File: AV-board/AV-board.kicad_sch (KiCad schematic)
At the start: 25 parts, among them J1 Mini-DIN-8, Q1 BC547, Q2 BC547, Q3 BC547, Q4 BC547, U2 74LS241

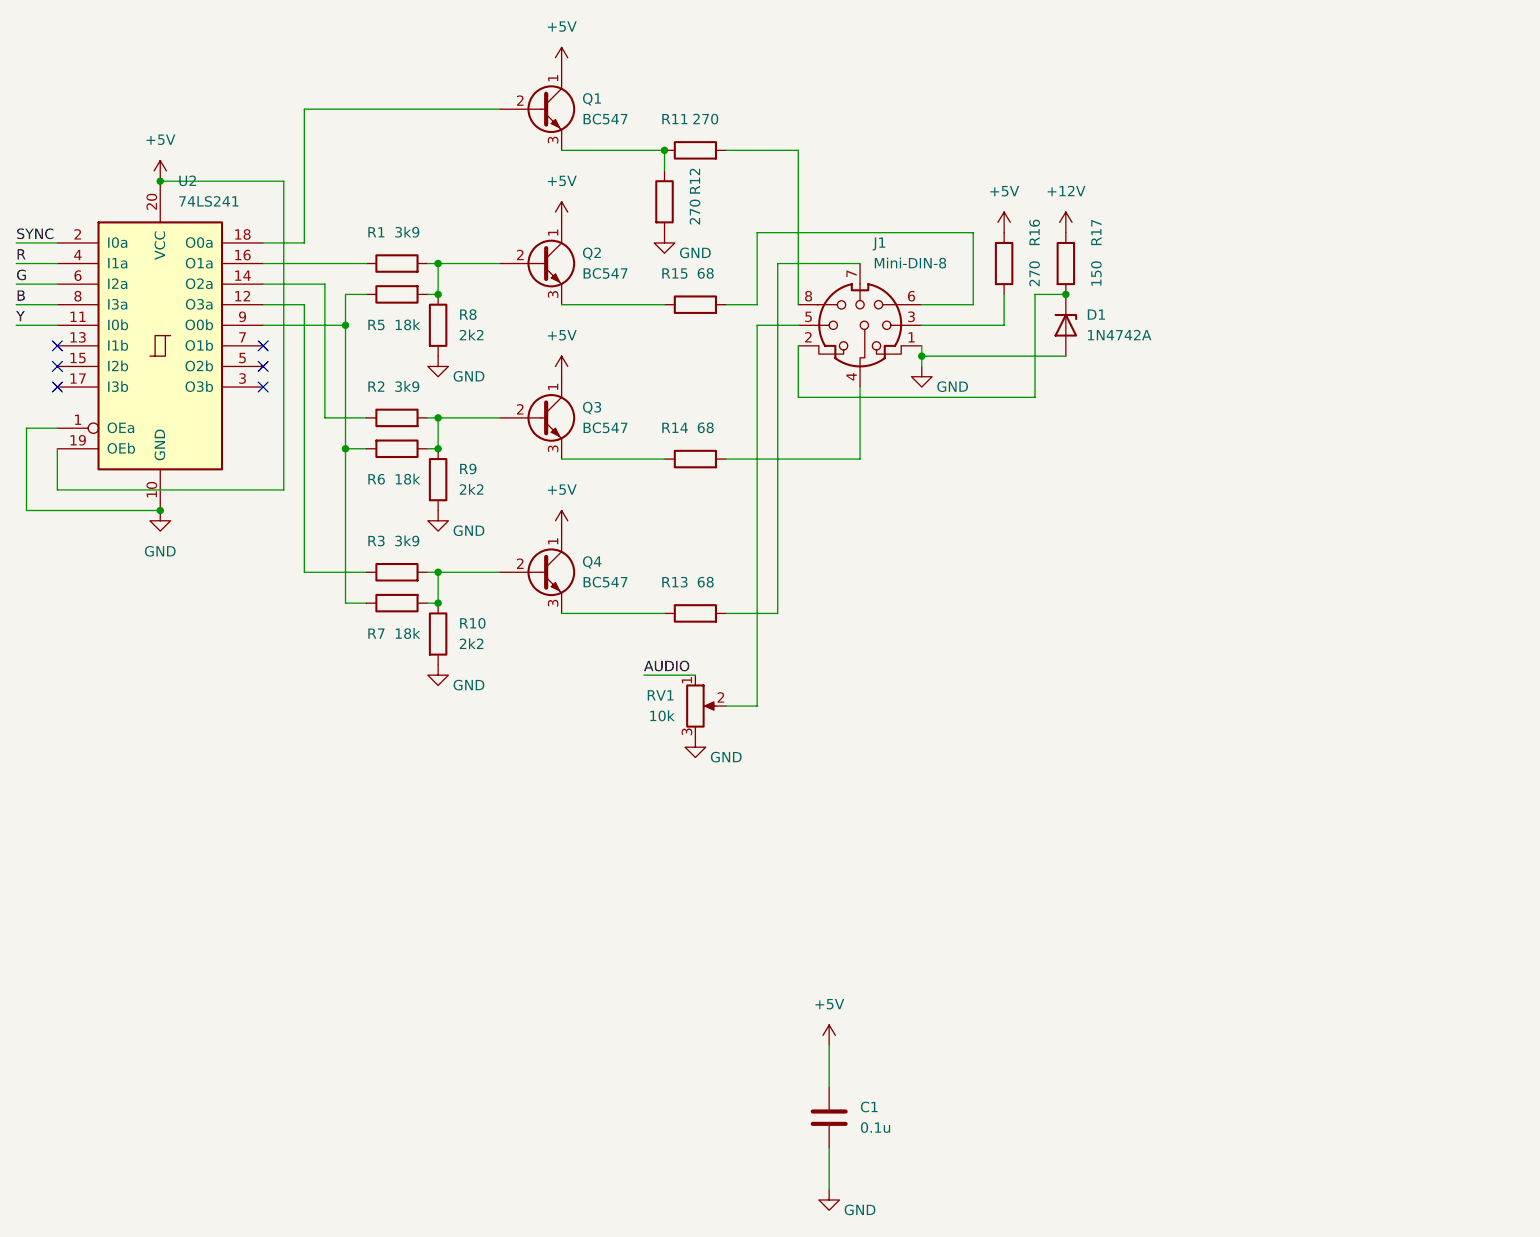
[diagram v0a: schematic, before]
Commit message: AudioVideo board like Harlequin for any ZX Clone
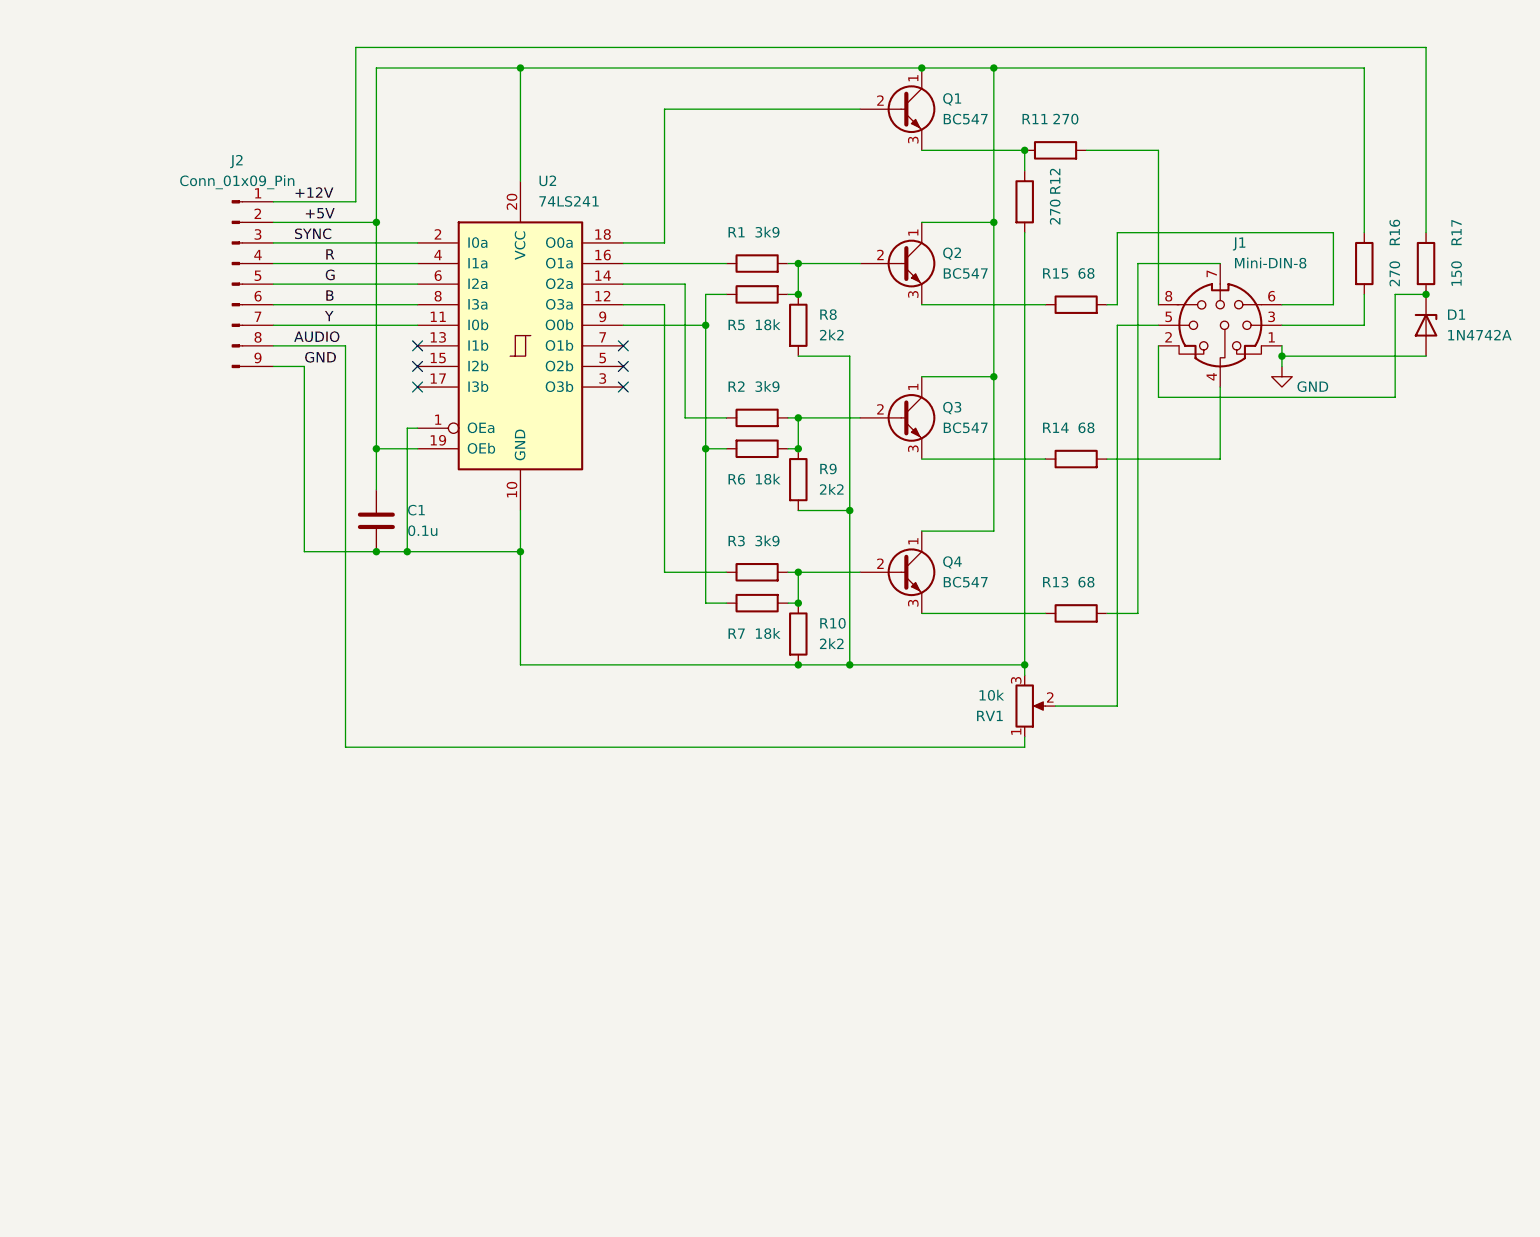
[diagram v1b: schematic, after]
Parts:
- added J2: Conn_01x09_Pin, Connector_PinHeader_2.54mm:PinHeader_1x09_P2.54mm_Vertical, symbol Connector:Conn_01x09_Pin
- RV1: footprint Potentiometer_THT:Potentiometer_ACP_CA9-V10_Vertical -> Potentiometer_THT:Potentiometer_Piher_PT-6-V_Vertical
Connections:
- net +12V: now also J2.1 (Pin_1)
- net +5V: now also J2.2 (Pin_2)
- net AUDIO: now also J2.8 (Pin_8)
- net B: now also J2.6 (Pin_6)
- net G: now also J2.5 (Pin_5)
- net GND: now also J2.9 (Pin_9)
- net R: now also J2.4 (Pin_4)
- net SYNC: now also J2.3 (Pin_3)
- net Y: now also J2.7 (Pin_7)
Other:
- moved on the sheet: C1, D1, J1, Q1, Q2, Q3, Q4, R1, R10, R11, R12, R13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

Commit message: Added capacitor to smooth interference
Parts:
- added C2: 680uF x 16v, Capacitor_THT:CP_Radial_D5.0mm_P2.50mm, symbol Device:C_Polarized
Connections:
- net +5V: now also C2.1
- net GND: now also C2.2
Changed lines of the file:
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@@
 (kicad_sch (version 20230121) (generator eeschema)
   (paper "A4")
+  (junction (at 93.98 95.25) (diameter 0) (color 0 0 0 0)
+  )
   (junction (at 107.95 50.8) (diameter 0) (color 0 0 0 0)
   )
@@
   )
   (junction (at 90.17 110.49) (diameter 0) (color 0 0 0 0)
+  )
+  (junction (at 107.95 62.23) (diameter 0) (color 0 0 0 0)
   )
   (junction (at 148.59 124.46) (diameter 0) (color 0 0 0 0)
@@
     (stroke (width 0) (type default))
   )
+  (wire (pts (xy 107.95 62.23) (xy 107.95 50.8))
+    (stroke (width 0) (type default))
+  )
   (wire (pts (xy 128.27 93.98) (xy 133.35 93.98))
     (stroke (width 0) (type default))
@@
     (stroke (width 0) (type default))
   )
+  (wire (pts (xy 104.14 62.23) (xy 107.95 62.23))
+    (stroke (width 0) (type default))
+  )
   (wire (pts (xy 184.15 74.93) (xy 184.15 118.11))
     (stroke (width 0) (type default))
@@
     (stroke (width 0) (type default))
   )
+  (wire (pts (xy 93.98 62.23) (xy 93.98 95.25))
+    (stroke (width 0) (type default))
+  )
   (wire (pts (xy 181.61 80.01) (xy 181.61 71.12))
     (stroke (width 0) (type default))
@@
     (stroke (width 0) (type default))
   )
-  (wire (pts (xy 107.95 64.77) (xy 107.95 50.8))
+  (wire (pts (xy 107.95 64.77) (xy 107.95 62.23))
     (stroke (width 0) (type default))
   )
@@
   )
   (wire (pts (xy 128.27 77.47) (xy 128.27 93.98))
+    (stroke (width 0) (type default))
+  )
+  (wire (pts (xy 96.52 62.23) (xy 93.98 62.23))
     (stroke (width 0) (type default))
   )
@@
         )
       )
+    )
+  )
+  (symbol (lib_id "Device:C_Polarized") (at 100.33 62.23 270) (unit 1)
+    (in_bom yes) (on_board yes) (dnp no) (fields_autoplaced)
+    (property "Reference" "C2" (at 101.219 54.61 90)
+      (effects (font (size 1.27 1.27)))
+    )
+    (property "Value" "680uF x 16v" (at 101.219 57.15 90)
+      (effects (font (size 1.27 1.27)))
+    )
+    (property "Footprint" "Capacitor_THT:CP_Radial_D5.0mm_P2.50mm" (at 96.52 63.1952 0)
+      (effects (font (size 1.27 1.27)) hide)
+    )
+    (property "Datasheet" "~" (at 100.33 62.23 0)
+      (effects (font (size 1.27 1.27)) hide)
+    )
+    (pin "1")
+    (pin "2")
+    (instances
+      (project "AV-board"
+        (path "/3953bd6e-ac12-488a-84a1-98577397b3fb"
+          (reference "C2") (unit 1)
+        )
+      )
